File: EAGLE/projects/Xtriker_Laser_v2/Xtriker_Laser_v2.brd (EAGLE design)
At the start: 127 x 101.3 mm, 142 parts, among them IC1 REG1117, IC2 LM358D, IC3 LM358D, IC4 LM358D, Q1 32,768K, Q2 8MHz, X1 USB_VCP, X4 MKDSN1,5/4-5,08, X6 MKDSN1,5/4-5,08, X7 MKDSN1,5/4-5,08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

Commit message: Cambios en tamaño de las pistas
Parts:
- moved Q1 1.27 mm to (53.3, 25.4)
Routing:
- net SWIO: track 0.00 -> 65.1 mm, vias 0 -> 1
- net GND: track 427.0 -> 491.8 mm, vias 3 -> 6
- net N$53: track 0.00 -> 54.9 mm, vias 0 -> 2
- net 3V: track 101.5 -> 154.6 mm, vias 2 -> 4
- net SWCLK: track 0.00 -> 51.9 mm, vias 0 -> 1
- net PWM_LASER: track 0.00 -> 45.3 mm, vias 0 -> 2
- net CONTROL_RESET: track 0.00 -> 38.5 mm
- net PROBE: track 0.00 -> 38.4 mm
- net CONTROL_FEED_HOLD_BIT: track 0.00 -> 38.2 mm
- net CONTROL_CYCLE_START_BIT: track 0.00 -> 38.1 mm, vias 0 -> 2
- net SAFETY_STOP: track 0.00 -> 37.5 mm
- net N$50: track 5.60 -> 38.0 mm, vias 0 -> 2
- net N$74: track 0.00 -> 29.7 mm, vias 0 -> 1
- net 12V: track 197.3 -> 223.8 mm, vias 0 -> 2
- net N$70: track 6.69 -> 24.9 mm, vias 0 -> 2
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
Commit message: Añadido pistas del Microcontrolador
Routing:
- net X_STEP: track 0.00 -> 90.8 mm, vias 0 -> 2
- net GND: track 491.8 -> 571.2 mm, vias 6 -> 7
- net N$40: track 5.42 -> 78.1 mm, vias 0 -> 2
- net N$17: track 0.00 -> 28.6 mm
- net RESET: track 18.0 -> 35.0 mm
- net ENDSTOP_Z: track 27.6 -> 31.4 mm
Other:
- outline, holes or cut-outs redrawn

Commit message: Pre terminado de inserción de pistas
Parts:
- moved R36 28.7 mm to (63.5, 40.6), flipped to the bottom, turned to 90 degrees
- moved R7 25.0 mm to (57.1, 38.1), turned to 90 degrees
- moved LED6 23.4 mm to (57.1, 33.0)
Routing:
- net 3V: track 154.6 -> 411.0 mm, vias 4 -> 15
- net GND: track 571.2 -> 777.8 mm, vias 7 -> 20
- net X_DIR: track 0.00 -> 186.2 mm, vias 0 -> 3
- net ENABLE: track 0.00 -> 172.8 mm, vias 0 -> 10
- net USB_5V: track 6.49 -> 112.4 mm, vias 0 -> 1
- net A_DIR: track 0.00 -> 88.0 mm, vias 0 -> 3
- net N$42: track 0.00 -> 82.2 mm, vias 0 -> 5
- net N$46: track 5.94 -> 74.8 mm, vias 0 -> 1
- net X_STEP: track 90.8 -> 159.1 mm, vias 2 -> 3
- net 12V: track 223.8 -> 290.2 mm, vias 2 -> 6
- net ENDSTOP_X: track 15.2 -> 78.6 mm, vias 0 -> 1
- net Z_DIR: track 0.00 -> 47.1 mm, vias 0 -> 2
- net MODE2: track 8.35 -> 54.0 mm, vias 1 -> 2
- net ENDSTOP_Y: track 21.7 -> 67.0 mm, vias 0 -> 3
- net ENDSTOP_Z: track 31.4 -> 75.0 mm, vias 0 -> 3
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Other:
- board size 127 x 101.3 mm -> 127 x 100 mm

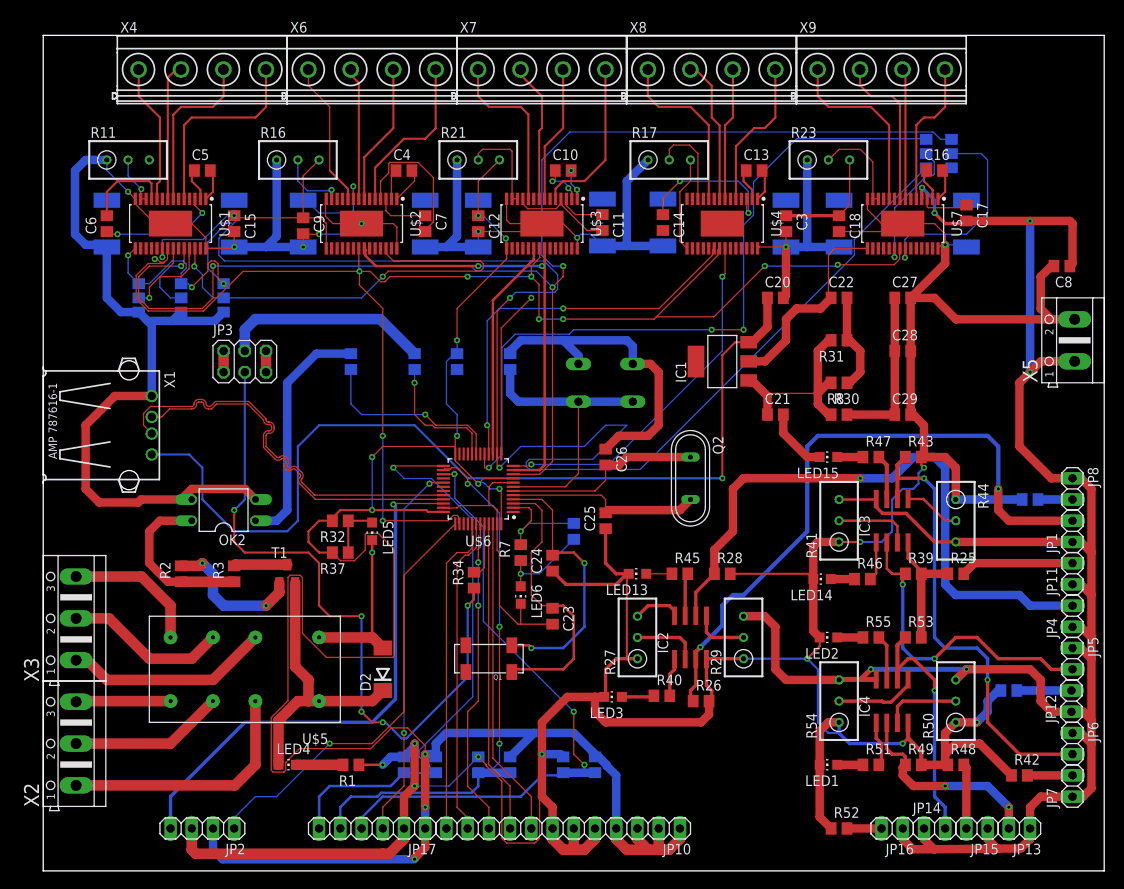
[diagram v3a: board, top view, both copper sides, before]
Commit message: Ruteado completo de la PCB
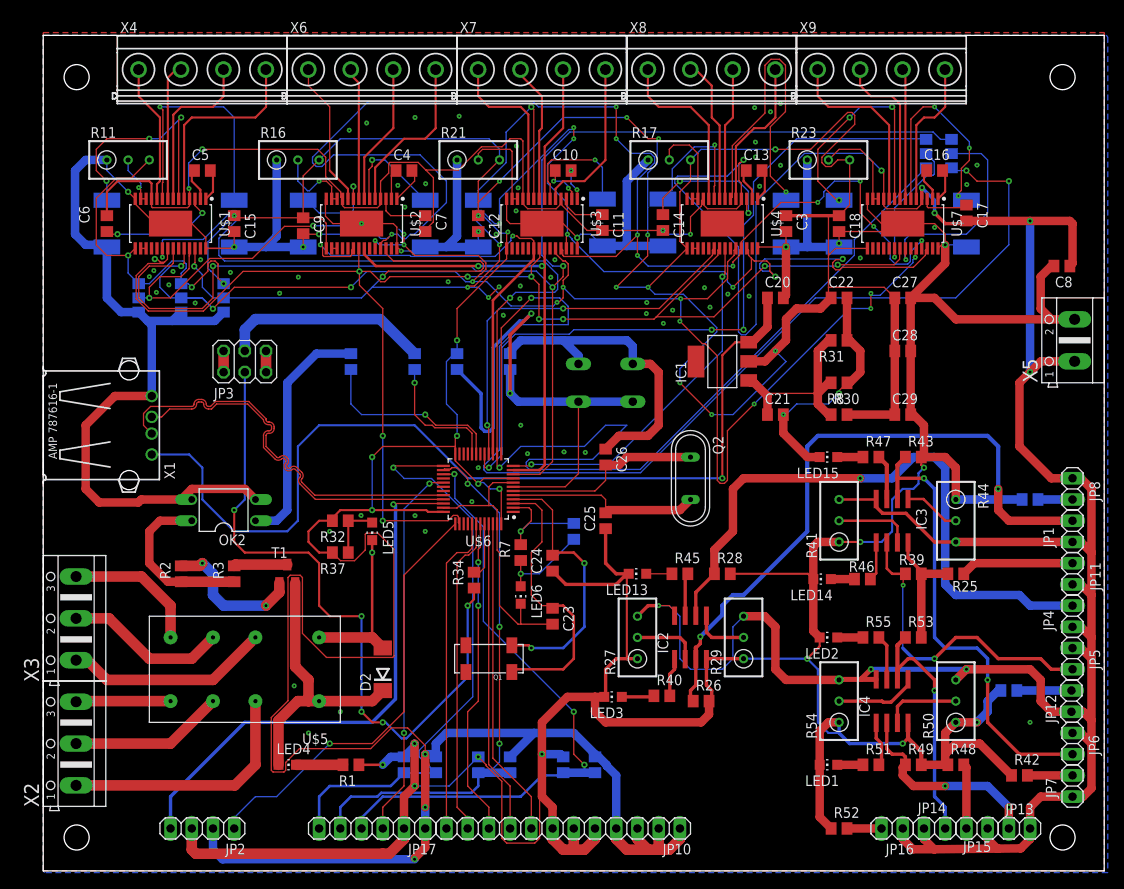
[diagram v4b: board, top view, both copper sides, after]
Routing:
- net MODE1: track 10.7 -> 200.0 mm, vias 1 -> 12
- net 12V: track 290.2 -> 475.2 mm, vias 6 -> 13
- net 3V: track 411.0 -> 595.4 mm, vias 15 -> 25
- net MODE0: track 9.66 -> 182.5 mm, vias 1 -> 15
- net MODE2: track 54.0 -> 179.3 mm, vias 2 -> 13
- net A_STEP: track 20.2 -> 141.5 mm, vias 1 -> 3
- net N$59: track 0.00 -> 38.4 mm, vias 0 -> 1
- net RESET: track 35.0 -> 71.5 mm, vias 0 -> 2
- net Y_DIR: track 26.6 -> 61.0 mm, vias 0 -> 2
- net N$37: track 0.00 -> 30.5 mm, vias 0 -> 1
- net N$67: track 0.00 -> 29.4 mm, vias 0 -> 3
- net N$27: track 0.00 -> 28.2 mm, vias 0 -> 3
- net N$66: track 0.00 -> 27.2 mm, vias 0 -> 3
- net N$26: track 0.00 -> 24.9 mm, vias 0 -> 1
- net N$60: track 0.00 -> 17.0 mm, vias 0 -> 1
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- added copper zone on layer 1, net GND
- added copper zone on layer 16, net GND
